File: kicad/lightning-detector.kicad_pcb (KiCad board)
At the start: 2 copper layers, 109.5 x 78.5 mm, 12 parts, among them J1 PWR, J3 Conn_01x03, U1 TFT_320x240, U3 TPS61023DRLR

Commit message: wk07 items
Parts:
- removed D1: LED, LED_THT:LED_D3.0mm
- removed U1: TFT_320x240, 3rdparty:TFT-320x240
- added J4: ADF7020 Breakout, Connector_IDC:IDC-Header_2x07_P2.54mm_Vertical, F.Cu at (182.7, 109.9)
- moved A2 55.5 mm to (177.1, 90.1)
- moved J3 51.4 mm to (170.7, 67.5), turned to -90 degrees
- moved BZ1 38.3 mm to (152.7, 72.0)
- moved L1 36.2 mm to (195.5, 71.3)
- moved J1 34.6 mm to (201.5, 67.6), turned to 180 degrees
- moved C1 24.9 mm to (192.5, 71.4), turned to 90 degrees
- moved U3 24.8 mm to (190.0, 71.2)
- moved R4 22.9 mm to (186.7, 75.0), turned to -90 degrees
- moved C4 17.2 mm to (186.7, 67.4), turned to 90 degrees
- moved R3 13.5 mm to (186.8, 71.3)
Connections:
- A2 pad 14: Net-(A2-GP10) -> /CLKOUT
- A2 pad 15: Net-(A2-GP11) -> /TXRXCLK
- A2 pad 16: Net-(A2-GP12) -> /TXRXDATA
- A2 pad 17: Net-(A2-GP13) -> /SWD_INT
- A2 pad 19: Net-(A2-GP14) -> /CE_70XX
- A2 pad 2: unconnected-(A2-GP1-Pad2) -> /ADC_IP
- A2 pad 20: Net-(A2-GP15) -> unconnected-(A2-GP15-Pad20)
- A2 pad 4: unconnected-(A2-GP2-Pad4) -> /SCLK
- A2 pad 5: unconnected-(A2-GP3-Pad5) -> /SREAD
- A2 pad 6: unconnected-(A2-GP4-Pad6) -> /SDATA
- A2 pad 7: unconnected-(A2-GP5-Pad7) -> /SLE
- A2 pad 9: unconnected-(A2-GP6-Pad9) -> /MUXOUT
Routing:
- net /SREAD: track 0.00 -> 73.8 mm
- net +3V3: track 0.00 -> 59.3 mm
- net /SCLK: track 0.00 -> 53.6 mm
- net /ADC_IP: track 0.00 -> 46.7 mm
- net /SLE: track 0.00 -> 38.2 mm
- net /SDATA: track 0.00 -> 35.2 mm
- net Net-(A2-GP0): track 0.00 -> 33.4 mm
- net /MUXOUT: track 0.00 -> 29.5 mm
- net /ADC_IN: track 0.00 -> 15.8 mm
- net /SWD_INT: track 0.00 -> 13.2 mm
- net +BATT: track 0.00 -> 12.6 mm
- net /TXRXCLK: track 0.00 -> 12.3 mm
- net GND: track 0.00 -> 12.1 mm, vias 0 -> 1
- net /TXRXDATA: track 0.00 -> 9.71 mm
- net /CLKOUT: track 0.00 -> 8.62 mm
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- added copper zone on F.Cu, net GND
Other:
- board size 109.5 x 78.5 mm -> 60.6 x 51.8 mm

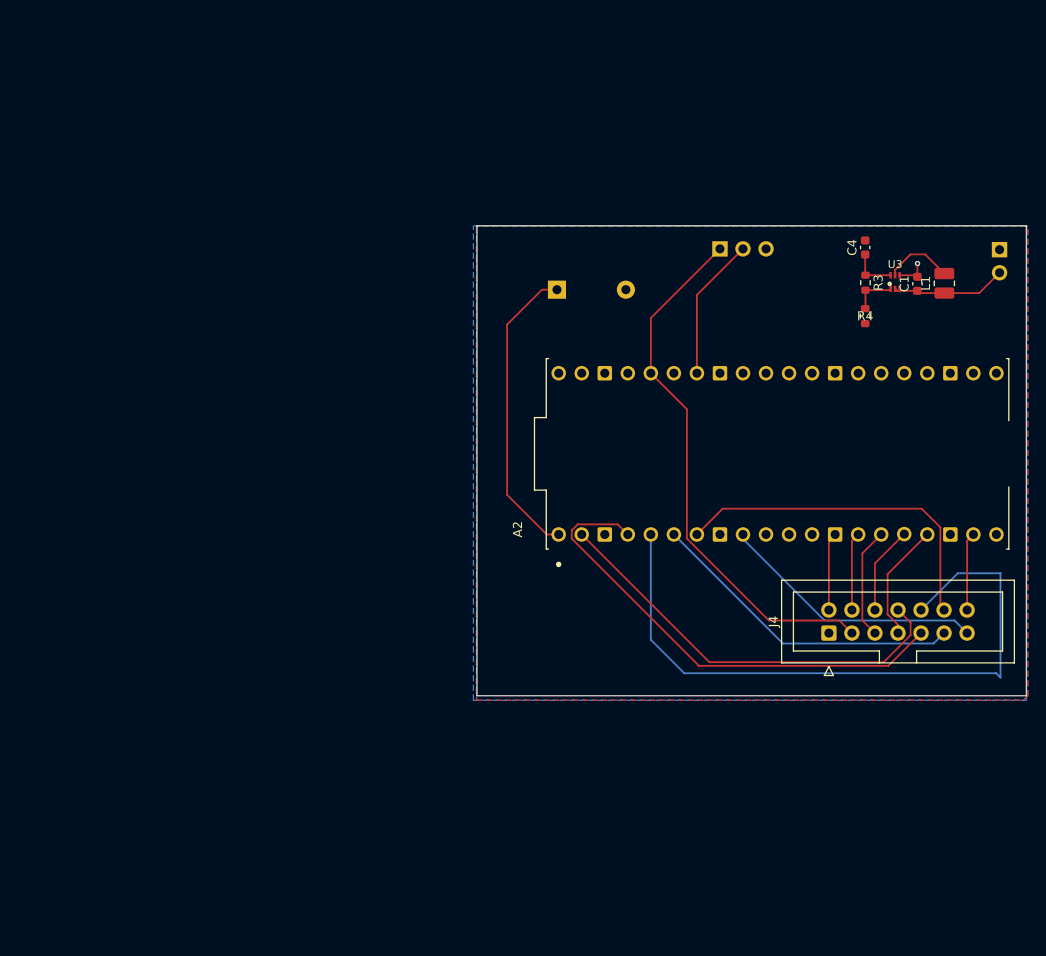
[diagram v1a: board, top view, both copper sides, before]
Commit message: v1.1, new schematic/pcb
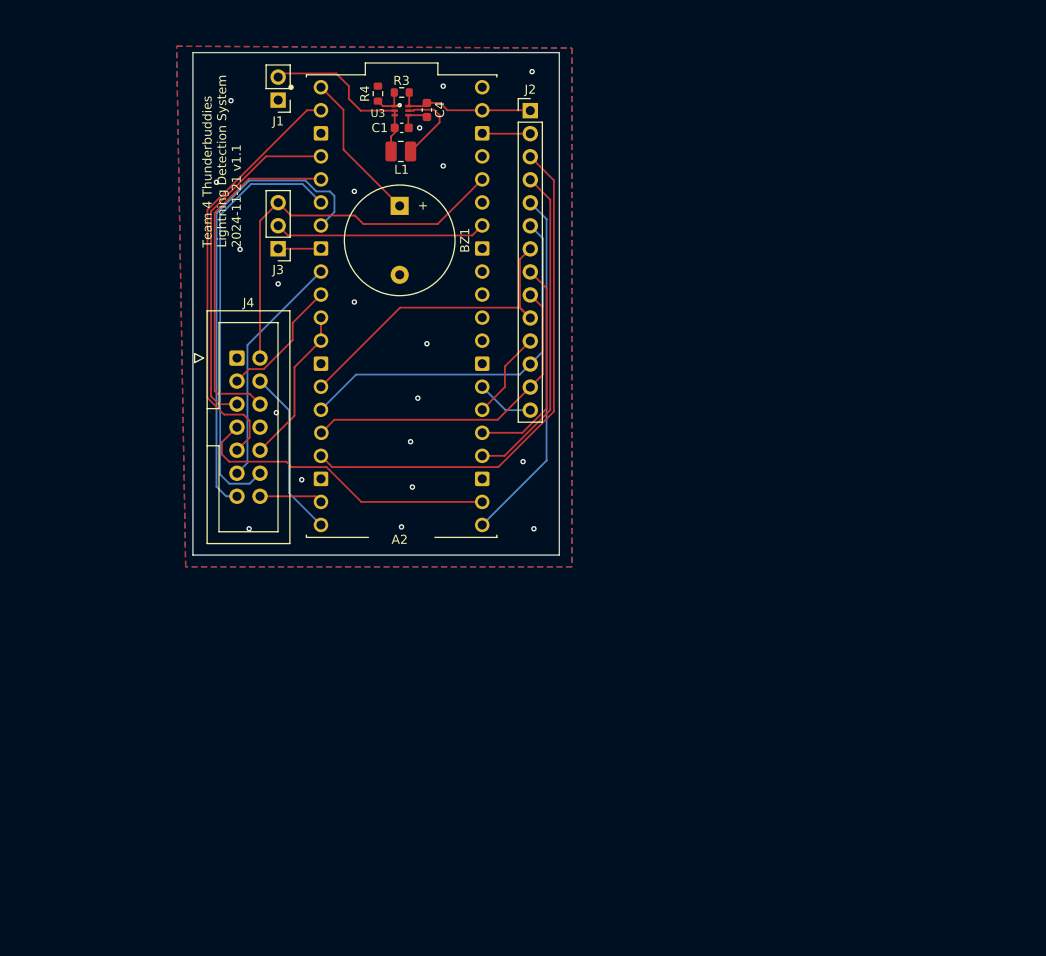
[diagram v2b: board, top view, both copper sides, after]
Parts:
- added J2: TFT LCD Display, Connector_PinHeader_2.54mm:PinHeader_1x14_P2.54mm_Vertical, F.Cu at (149.8, 52.3)
- A2: footprint 3rdparty:MODULE_SC0918 -> PicoW:MODULE_SC0918
- BZ1, J1, J3: moved to F.Cu
- U3: footprint 3rdparty:SOT563-ORI -> ThunderBuddies_Lib:SOT563-ORI
- moved J1 81.2 mm to (122.0, 51.1)
- moved J4 72.0 mm to (117.5, 79.6), turned to 0 degrees
- moved L1 61.7 mm to (135.5, 56.8), turned to 0 degrees
- moved C1 59.4 mm to (135.6, 54.2), turned to 0 degrees
- moved R4 59.1 mm to (133.0, 50.4), turned to 90 degrees
- moved U3 57.6 mm to (135.6, 52.3), turned to -90 degrees
- moved R3 55.3 mm to (135.6, 50.3), turned to 180 degrees
- moved C4 50.6 mm to (138.4, 52.2), turned to -90 degrees
- moved J3 48.7 mm to (122.0, 67.5), turned to 180 degrees
- moved A2 44.5 mm to (135.6, 73.8), turned to 0 degrees
- moved BZ1 19.6 mm to (135.4, 62.8), turned to -90 degrees
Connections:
- A2 pad 10: unconnected-(A2-GP7-Pad10) -> /DATA_CLK
- A2 pad 11: unconnected-(A2-GP8-Pad11) -> /DATA I/O
- A2 pad 12: unconnected-(A2-GP9-Pad12) -> /DATA I/O
- A2 pad 14: /CLKOUT -> /TFT_SCK
- A2 pad 15: /TXRXCLK -> /TFT_SDI
- A2 pad 16: /TXRXDATA -> /TFT_SDO
- A2 pad 17: /SWD_INT -> /TFT_CS
- A2 pad 2: /ADC_IP -> /CLKOUT
- A2 pad 20: unconnected-(A2-GP15-Pad20) -> /INT/LOCK
- A2 pad 21: unconnected-(A2-GP16-Pad21) -> /TFT_DC
- A2 pad 22: unconnected-(A2-GP17-Pad22) -> /MUXOUT
- A2 pad 24: unconnected-(A2-GP18-Pad24) -> /TFT_RST
- A2 pad 25: unconnected-(A2-GP19-Pad25) -> /TFT_LED
- A2 pad 26: unconnected-(A2-GP20-Pad26) -> /TFT_TOUCH_CS
- A2 pad 27: unconnected-(A2-GP21-Pad27) -> /TFT_IRQ
- A2 pad 5: /SREAD -> /SDATA
- A2 pad 6: /SDATA -> /SREAD
- A2 pad 9: /MUXOUT -> /ADF_ADCINP
- J3 pad 1: +3V3 -> GND
- J3 pad 3: GND -> +3V3
- J4 pad 10: /SREAD -> /DATA I/O
- J4 pad 11: /SDATA -> /ADF_ADCINP
- J4 pad 12: /SLE -> /SREAD
- J4 pad 13: /MUXOUT -> /SLE
- J4 pad 2: GND -> +3V3
- J4 pad 3: +3V3 -> /DATA_CLK
- J4 pad 4: /CLKOUT -> /INT/LOCK
- J4 pad 5: /TXRXCLK -> /SCLK
- J4 pad 6: /TXRXDATA -> /SDATA
- J4 pad 7: /SWD_INT -> /MUXOUT
- J4 pad 8: /ADC_IP -> GND
- J4 pad 9: /SCLK -> /CLKOUT
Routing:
- net /TFT_CS: track 0.00 -> 57.9 mm
- net /ADC_IP: track 46.7 -> 0.00 mm
- net /TFT_SDI: track 0.00 -> 41.6 mm
- net /TFT_DC: track 0.00 -> 39.2 mm
- net /CLKOUT: track 8.62 -> 47.3 mm
- net /TFT_SDO: track 0.00 -> 36.4 mm
- net /TFT_RST: track 0.00 -> 35.9 mm
- net /TFT_SCK: track 0.00 -> 35.7 mm
- net /SREAD: track 73.8 -> 47.3 mm
- net /ADF_ADCINP: track 0.00 -> 26.1 mm
- net /TFT_LED: track 0.00 -> 24.0 mm
- net /INT/LOCK: track 0.00 -> 18.6 mm
- net /DATA I/O: track 0.00 -> 17.4 mm
- net Net-(A2-GP0): track 33.4 -> 16.7 mm
- net +3V3: track 59.3 -> 43.5 mm
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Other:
- board size 60.6 x 51.8 mm -> 40.4 x 55.4 mm
- board text added: "Team 4 Thunderbuddies Lightning Detection System 2024-11-21 v1.1"

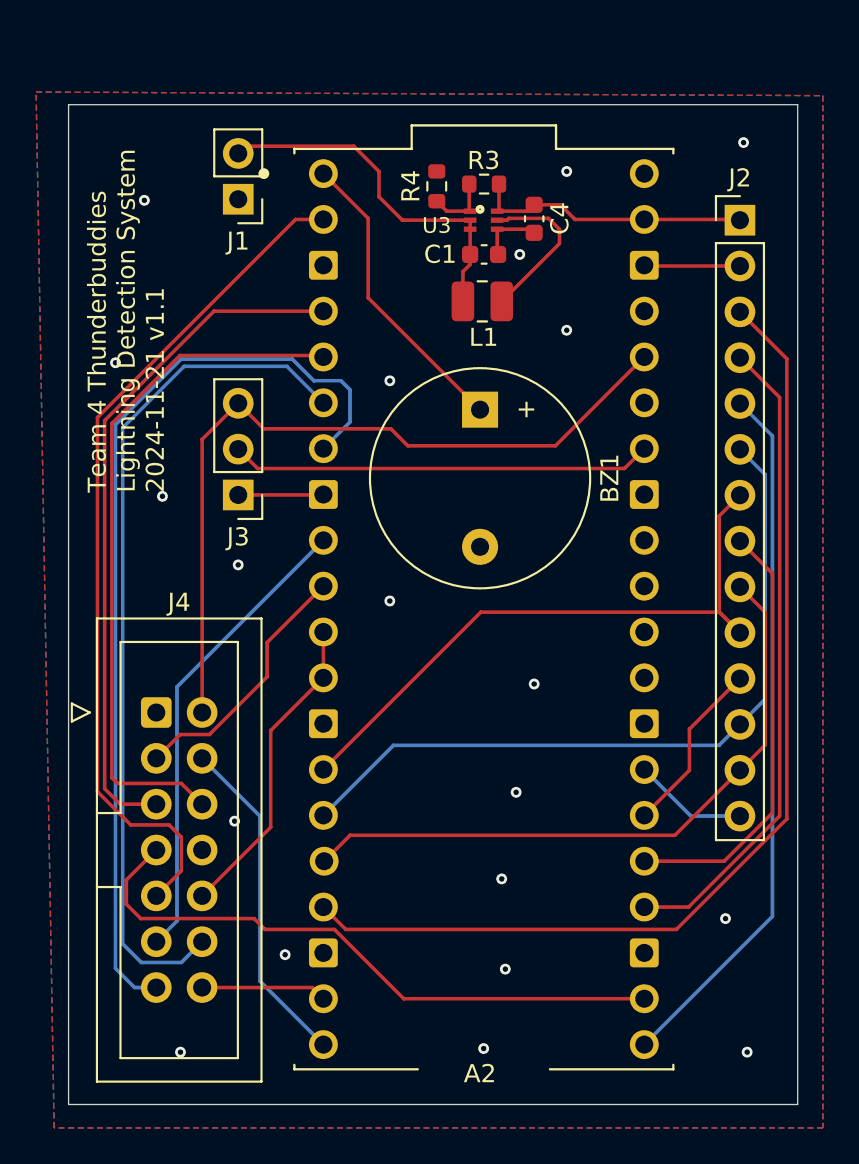
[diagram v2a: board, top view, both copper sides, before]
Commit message: add mounting holes
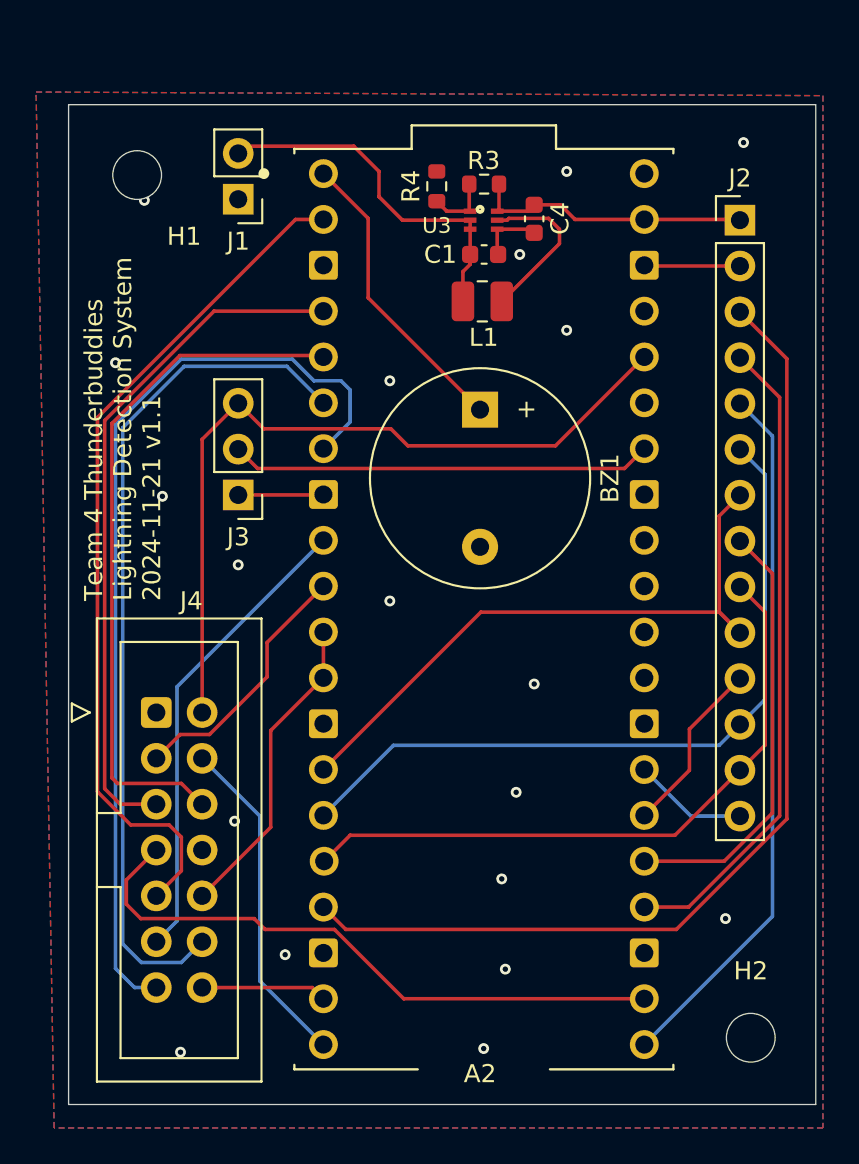
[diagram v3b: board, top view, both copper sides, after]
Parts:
- added H1: MountingHole, MountingHole:MountingHole_2.7mm_M2.5, F.Cu at (116.4, 49.8)
- added H2: MountingHole, MountingHole:MountingHole_2.7mm_M2.5, F.Cu at (150.4, 97.6)
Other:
- board size 40.4 x 55.4 mm -> 41.4 x 55.4 mm
